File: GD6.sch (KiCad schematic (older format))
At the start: 19 parts, among them IC5 HCPL-316J, IC6 IXDD614PI, P12 CONN_01X03, P13 CONN_01X03

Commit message: uding HCPL-361J modified symbol
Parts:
- IC5: symbol HCPL-316J-RESCUE-gatedrive -> HCPL-316J
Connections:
- wire segments 41 -> 54
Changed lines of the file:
@@
 EESchema Schematic File Version 2
-LIBS:gatedrive-rescue
 LIBS:power
 LIBS:device
@@
 LIBS:contrib
 LIBS:valves
-LIBS:GateDrive
+LIBS:74xgxx
+LIBS:ac-dc
+LIBS:actel
+LIBS:Altera
+LIBS:analog_devices
+LIBS:brooktre
+LIBS:cmos_ieee
+LIBS:dc-dc
+LIBS:diode
+LIBS:elec-unifil
+LIBS:ESD_Protection
+LIBS:ftdi
+LIBS:gennum
+LIBS:graphic
+LIBS:hc11
+LIBS:ir
+LIBS:Lattice
+LIBS:logo
+LIBS:maxim
+LIBS:microchip_dspic33dsc
+LIBS:microchip_pic10mcu
+LIBS:microchip_pic12mcu
+LIBS:microchip_pic16mcu
+LIBS:microchip_pic18mcu
+LIBS:microchip_pic32mcu
+LIBS:motor_drivers
+LIBS:msp430
+LIBS:nordicsemi
+LIBS:nxp_armmcu
+LIBS:onsemi
+LIBS:Oscillators
+LIBS:powerint
+LIBS:Power_Management
+LIBS:pspice
+LIBS:references
+LIBS:relays
+LIBS:rfcom
+LIBS:sensors
+LIBS:silabs
+LIBS:stm8
+LIBS:stm32
+LIBS:supertex
+LIBS:switches
+LIBS:transf
+LIBS:ttl_ieee
+LIBS:video
+LIBS:Worldsemi
+LIBS:Xicor
+LIBS:Zilog
 LIBS:gatedrive-cache
 EELAYER 25 0
@@
 U 1 1 56EF8B77
 P 7900 5100
+AR Path="/56EF8B77" Ref="IC6"  Part="1"
+AR Path="/56EF0565/56EF8B77" Ref="IC6"  Part="1"
 F 0 "IC6" H 7900 4900 60  0000 C CNN
 F 1 "IXDD614PI" H 7950 5450 60  0000 C CNN
@@
 $EndComp
 $Comp
-L HCPL-316J-RESCUE-gatedrive IC5
+L HCPL-316J IC5
 U 1 1 56EF8B78
-P 5550 4750
-F 0 "IC5" H 5550 4150 60  0000 C CNN
-F 1 "HCPL-316J" H 5300 5200 60  0000 C CNN
-F 2 "Housings_SOIC:SOIC-16_7.5x10.3mm_Pitch1.27mm" H 5550 4750 60  0001 C CNN
-F 3 "" H 5550 4750 60  0000 C CNN
-F 4 "CHINA [ already bought]" H 5550 4750 60  0001 C CNN "Supplier"
-	1    5550 4750
+P 5700 4850
+F 0 "IC5" H 5700 4250 60  0000 C CNN
+F 1 "HCPL-316J" H 5450 5300 60  0000 C CNN
+F 2 "Housings_SOIC:SOIC-16_7.5x10.3mm_Pitch1.27mm" H 5700 4850 60  0001 C CNN
+F 3 "" H 5700 4850 60  0000 C CNN
+F 4 "CHINA [ already bought]" H 5700 4850 60  0001 C CNN "Supplier"
+	1    5700 4850
 	1    0    0    -1
 $EndComp
@@
 Text GLabel 7500 5150 0    60   Input ~ 0
 -5V6
-Text GLabel 8350 5150 2    60   Input ~ 0
+Text GLabel 8250 5150 2    60   Input ~ 0
 -5V6
 Text GLabel 10200 4950 2    60   Output ~ 0
@@
 a cap to ensure soft turn-off, recommended by datasheet of hcpl.
 Wire Wire Line
-	6950 4950 7500 4950
-Wire Wire Line
-	6250 4950 6650 4950
-Wire Wire Line
-	6250 5050 6250 5150
-Wire Wire Line
-	6250 4750 6250 4850
+	6950 4950 7150 4950
+Wire Wire Line
+	7150 4950 7500 4950
+Wire Wire Line
+	5900 4950 6500 4950
+Wire Wire Line
+	6500 4950 6650 4950
+Wire Wire Line
+	6250 5050 6250 5100
+Wire Wire Line
+	6250 5100 6250 5150
+Wire Wire Line
+	6250 4750 6250 4800
+Wire Wire Line
+	6250 4800 6250 4850
 Connection ~ 6550 4100
 Wire Wire Line
-	6550 4650 6250 4650
+	6550 4650 5900 4650
 Wire Wire Line
 	6550 4100 6650 4100
 Wire Wire Line
-	6550 4050 6550 4650
+	6550 4050 6550 4100
+Wire Wire Line
+	6550 4100 6550 4650
 Connection ~ 8450 4950
 Wire Wire Line
@@
 Connection ~ 7150 4950
 Wire Wire Line
-	3625 4650 4850 4650
-Wire Wire Line
-	8350 4950 9050 4950
+	3625 4650 4000 4650
+Wire Wire Line
+	4000 4650 5000 4650
+Wire Wire Line
+	8250 4950 8450 4950
+Wire Wire Line
+	8450 4950 8900 4950
+Wire Wire Line
+	8900 4950 9050 4950
 Wire Wire Line
 	9350 4950 9450 4950
 Wire Wire Line
-	9750 4950 10200 4950
+	9750 4950 9950 4950
+Wire Wire Line
+	9950 4950 10200 4950
 Wire Wire Line
 	9750 5250 9950 5250
@@
 Connection ~ 9950 4950
 Wire Wire Line
-	8350 5050 8450 5050
+	8250 5050 8450 5050
 Wire Wire Line
 	8450 5050 8450 4950
@@
 	4400 4350 4400 4550
 Wire Wire Line
-	4400 4550 4850 4550
+	4400 4550 5000 4550
 Wire Wire Line
 	4000 4350 4000 4650
@@
 	4000 5300 4000 4750
 Wire Wire Line
-	4000 4750 4850 4750
-Wire Wire Line
-	4850 5150 4750 5150
+	4000 4750 5000 4750
+Wire Wire Line
+	5000 5150 4750 5150
 Wire Wire Line
 	4750 5150 4750 5300
 Wire Wire Line
-	4850 4850 4400 4850
+	5000 4850 4400 4850
 Wire Wire Line
 	4400 4850 4400 5300
 Wire Wire Line
-	6250 4450 6300 4450
+	5900 4450 6300 4450
 Wire Wire Line
 	6300 4450 6300 4350
@@
 Wire Wire Line
 	6500 5000 6500 4950
-Text GLabel 8350 4850 2    60   Input ~ 0
+Text GLabel 8250 4850 2    60   Input ~ 0
 15V6
 Text GLabel 7025 5125 3    60   Input ~ 0
@@
 Text HLabel 900  3800 3    60   Input ~ 0
 T6
-Text HLabel 4850 4450 0    60   Input ~ 0
+Text HLabel 5000 4450 0    60   Input ~ 0
 T6
 Text GLabel 4450 2300 3    60   Input ~ 0
@@
 Text GLabel 4400 4350 1    60   Input ~ 0
 GND1
-Text GLabel 4850 4950 0    60   Input ~ 0
+Text GLabel 5000 4950 0    60   Input ~ 0
 ~FAULT
 Text GLabel 4750 5300 3    60   Input ~ 0
@@
 Text GLabel 1275 5325 2    60   Input ~ 0
 COM6
+Wire Wire Line
+	6250 4850 5900 4850
+Wire Wire Line
+	6250 4750 5900 4750
+Wire Wire Line
+	6250 5050 5900 5050
+Wire Wire Line
+	6250 5150 5900 5150
 $EndSCHEMATC

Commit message: cleaning the schematic
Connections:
- wire segments 54 -> 45
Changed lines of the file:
@@
 a cap to ensure soft turn-off, recommended by datasheet of hcpl.
 Wire Wire Line
-	6950 4950 7150 4950
+	6950 4950 7500 4950
 Wire Wire Line
-	7150 4950 7500 4950
+	5900 4950 6650 4950
 Wire Wire Line
-	5900 4950 6500 4950
+	6250 5050 6250 5150
 Wire Wire Line
-	6500 4950 6650 4950
-Wire Wire Line
-	6250 5050 6250 5100
-Wire Wire Line
-	6250 5100 6250 5150
-Wire Wire Line
-	6250 4750 6250 4800
-Wire Wire Line
-	6250 4800 6250 4850
+	6250 4750 6250 4850
 Connection ~ 6550 4100
 Wire Wire Line
@@
 	6550 4100 6650 4100
 Wire Wire Line
-	6550 4050 6550 4100
-Wire Wire Line
-	6550 4100 6550 4650
+	6550 4050 6550 4650
 Connection ~ 8450 4950
 Wire Wire Line
@@
 Connection ~ 7150 4950
 Wire Wire Line
-	3625 4650 4000 4650
+	3625 4650 5000 4650
 Wire Wire Line
-	4000 4650 5000 4650
-Wire Wire Line
-	8250 4950 8450 4950
-Wire Wire Line
-	8450 4950 8900 4950
-Wire Wire Line
-	8900 4950 9050 4950
+	8250 4950 9050 4950
 Wire Wire Line
 	9350 4950 9450 4950
 Wire Wire Line
-	9750 4950 9950 4950
-Wire Wire Line
-	9950 4950 10200 4950
+	9750 4950 10200 4950
 Wire Wire Line
 	9750 5250 9950 5250

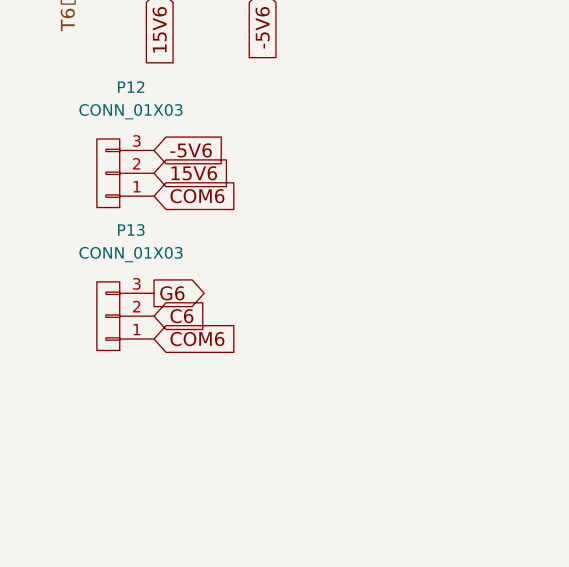
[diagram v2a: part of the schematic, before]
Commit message: completion of the layout, initial layout of the protection circuit, reducing number of circuit to 7
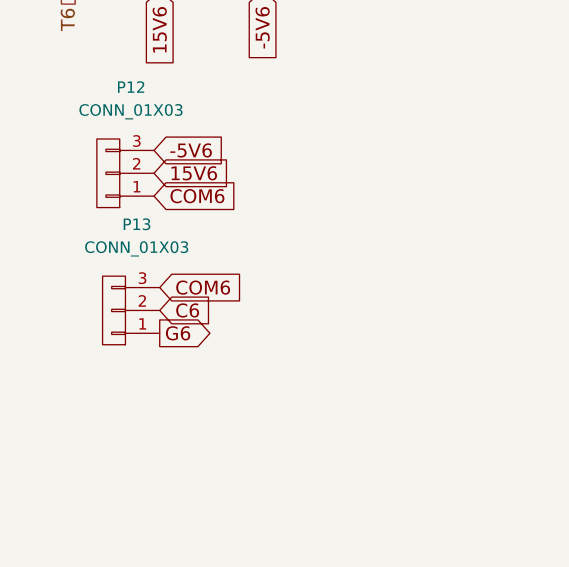
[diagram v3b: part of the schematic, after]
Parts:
- C15, C16, C17, C19, C20, C21: footprint Capacitors_ThroughHole:C_Disc_D3_P2.5 -> gatedrive:C_Disc
- D5: footprint Diodes_ThroughHole:Diode_DO-201AD_Horizontal_RM15 -> Diodes_ThroughHole:Diode_DO-41_SOD81_Horizontal_RM10
- R13: footprint Resistors_ThroughHole:Resistor_Vertical_RM5mm -> Resistors_ThroughHole:Resistor_Horizontal_RM10mm
- R17, R18: footprint Resistors_ThroughHole:Resistor_Horizontal_RM20mm -> gatedrive:Resistor_multi
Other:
- moved on the sheet: P13
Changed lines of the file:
@@
 EESchema Schematic File Version 2
+LIBS:Symbols_DCDC-ACDC-Converter_RevC_20Jul2012
+LIBS:Symbols_EN60617_13Mar2013
+LIBS:Symbols_EN60617-10_HF-Radio_DRAFT_12Sep2013
+LIBS:Symbols_ICs-Diskrete_RevD10
+LIBS:Symbols_ICs-Opto_RevB_16Sep2013
+LIBS:Symbols_Microcontroller_Philips-NXP_RevA_06Oct2013
+LIBS:SymbolsSimilarEN60617+oldDIN617-RevE8
+LIBS:Symbols_Socket-DIN41612_RevA
+LIBS:Symbols_Transformer-Diskrete_RevA
 LIBS:power
 LIBS:device
@@
 $Descr A4 11693 8268
 encoding utf-8
-Sheet 4 10
+Sheet 4 9
 Title "IGBT GATE DRIVE SCHEMATIC."
 Date "2016-03-02"
@@
 F 0 "D5" H 7150 3976 50  0000 C CNN
 F 1 "RGPO2-20" H 7150 3900 50  0000 C CNN
-F 2 "Diodes_ThroughHole:Diode_DO-201AD_Horizontal_RM15" H 7150 4100 50  0001 C CNN
+F 2 "Diodes_ThroughHole:Diode_DO-41_SOD81_Horizontal_RM10" H 7150 4100 50  0001 C CNN
 F 3 "" H 7150 4100 50  0000 C CNN
 F 4 "El-Amir" H 7150 4100 60  0001 C CNN "Supplier"
@@
 F 0 "R13" V 3525 4500 50  0000 C CNN
 F 1 "10K" V 3625 4500 50  0000 C CNN
-F 2 "Resistors_ThroughHole:Resistor_Vertical_RM5mm" V 3555 4500 50  0001 C CNN
+F 2 "Resistors_ThroughHole:Resistor_Horizontal_RM10mm" V 3555 4500 50  0001 C CNN
 F 3 "" H 3625 4500 50  0000 C CNN
 F 4 "EL AMIR" H 3625 4500 60  0001 C CNN "Supplier"
@@
 F 0 "C15" H 4150 2150 50  0000 C CNN
 F 1 "0.1uF" H 4250 2050 50  0000 C CNN
-F 2 "Capacitors_ThroughHole:C_Disc_D3_P2.5" H 4488 2000 50  0001 C CNN
+F 2 "gatedrive:C_Disc" H 4488 2000 50  0001 C CNN
 F 3 "" H 4450 2150 50  0000 C CNN
 F 4 "EL AMIR" H 4450 2150 60  0001 C CNN "Supplier"
@@
 F 0 "C17" H 7000 3900 50  0000 C CNN
 F 1 "100pF" H 6800 3900 50  0000 C CNN
-F 2 "Capacitors_ThroughHole:C_Disc_D3_P2.5" H 6588 3750 50  0001 C CNN
+F 2 "gatedrive:C_Disc" H 6588 3750 50  0001 C CNN
 F 3 "" H 6550 3900 50  0000 C CNN
 	1    6550 3900
@@
 F 0 "C21" H 8450 2150 50  0000 C CNN
 F 1 "0.1uF" H 8450 2050 50  0000 C CNN
-F 2 "Capacitors_ThroughHole:C_Disc_D3_P2.5" H 8888 2000 50  0001 C CNN
+F 2 "gatedrive:C_Disc" H 8888 2000 50  0001 C CNN
 F 3 "" H 8850 2150 50  0000 C CNN
 	1    8850 2150
@@
 F 0 "C20" H 7400 2150 50  0000 C CNN
 F 1 "0.1uF" H 7400 2050 50  0000 C CNN
-F 2 "Capacitors_ThroughHole:C_Disc_D3_P2.5" H 7788 2000 50  0001 C CNN
+F 2 "gatedrive:C_Disc" H 7788 2000 50  0001 C CNN
 F 3 "" H 7750 2150 50  0000 C CNN
 	1    7750 2150
@@
 F 0 "C16" H 5150 2150 50  0000 C CNN
 F 1 "0.1uF" H 5150 2050 50  0000 C CNN
-F 2 "Capacitors_ThroughHole:C_Disc_D3_P2.5" H 5538 2000 50  0001 C CNN
+F 2 "gatedrive:C_Disc" H 5538 2000 50  0001 C CNN
 F 3 "" H 5500 2150 50  0000 C CNN
 	1    5500 2150
@@
 LEFT OPEN OR CONNECTED TO THE VCC.
 $Comp
-L PWR_FLAG #FLG015
+L PWR_FLAG #FLG08
 U 1 1 56EF8B85
 P 1300 3800
-F 0 "#FLG015" H 1300 3895 50  0001 C CNN
+F 0 "#FLG08" H 1300 3895 50  0001 C CNN
 F 1 "PWR_FLAG" H 1300 4024 50  0000 C CNN
 F 2 "" H 1300 3800 50  0000 C CNN
@@
 $EndComp
 $Comp
-L PWR_FLAG #FLG016
+L PWR_FLAG #FLG09
 U 1 1 56EF8B86
 P 1750 3800
-F 0 "#FLG016" H 1750 3895 50  0001 C CNN
+F 0 "#FLG09" H 1750 3895 50  0001 C CNN
 F 1 "PWR_FLAG" H 1750 4024 50  0000 C CNN
 F 2 "" H 1750 3800 50  0000 C CNN
@@
 $EndComp
 $Comp
-L PWR_FLAG #FLG017
+L PWR_FLAG #FLG010
 U 1 1 56EF8B87
 P 1750 2650
-F 0 "#FLG017" H 1750 2745 50  0001 C CNN
+F 0 "#FLG010" H 1750 2745 50  0001 C CNN
 F 1 "PWR_FLAG" H 1750 2874 50  0000 C CNN
 F 2 "" H 1750 2650 50  0000 C CNN
@@
 $EndComp
 $Comp
-L PWR_FLAG #FLG018
+L PWR_FLAG #FLG011
 U 1 1 56EF8B88
 P 900 2650
-F 0 "#FLG018" H 900 2745 50  0001 C CNN
+F 0 "#FLG011" H 900 2745 50  0001 C CNN
 F 1 "PWR_FLAG" H 900 2874 50  0000 C CNN
 F 2 "" H 900 2650 50  0000 C CNN
@@
 $EndComp
 $Comp
-L PWR_FLAG #FLG019
+L PWR_FLAG #FLG012
 U 1 1 56EF8B89
 P 1300 2650
-F 0 "#FLG019" H 1300 2745 50  0001 C CNN
+F 0 "#FLG012" H 1300 2745 50  0001 C CNN
 F 1 "PWR_FLAG" H 1300 2874 50  0000 C CNN
 F 2 "" H 1300 2650 50  0000 C CNN
@@
 $EndComp
 $Comp
-L PWR_FLAG #FLG020
+L PWR_FLAG #FLG013
 U 1 1 56EF8B8A
 P 900 3800
-F 0 "#FLG020" H 900 3895 50  0001 C CNN
+F 0 "#FLG013" H 900 3895 50  0001 C CNN
 F 1 "PWR_FLAG" H 900 4024 50  0000 C CNN
 F 2 "" H 900 3800 50  0000 C CNN
@@
 F 0 "C19" H 7390 4630 50  0000 C CNN
 F 1 "10nF" H 7400 4550 50  0000 C CNN
-F 2 "Capacitors_ThroughHole:C_Disc_D3_P2.5" H 7188 4450 50  0001 C CNN
+F 2 "gatedrive:C_Disc" H 7188 4450 50  0001 C CNN
 F 3 "" H 7150 4600 50  0000 C CNN
 	1    7150 4600
@@
 F 0 "R17" V 9600 4980 50  0000 C CNN
 F 1 "60" V 9500 4950 50  0000 C CNN
-F 2 "Resistors_ThroughHole:Resistor_Horizontal_RM20mm" V 9530 4950 50  0001 C CNN
+F 2 "gatedrive:Resistor_multi" V 9530 4950 50  0001 C CNN
 F 3 "" H 9600 4950 50  0000 C CNN
 F 4 "Al amir" H 9600 4950 60  0001 C CNN "Supplier"
@@
 F 0 "R18" V 9600 5240 50  0000 C CNN
 F 1 "30ohm ,0.5W" V 9500 5250 50  0000 C CNN
-F 2 "Resistors_ThroughHole:Resistor_Horizontal_RM20mm" V 9530 5250 50  0001 C CNN
+F 2 "gatedrive:Resistor_multi" V 9530 5250 50  0001 C CNN
 F 3 "" H 9600 5250 50  0000 C CNN
 F 4 "Supplier_name" H 9600 5250 60  0001 C CNN "Supplier"
@@
 	6950 4100 7000 4100
 $Comp
-L PWR_FLAG #FLG021
+L PWR_FLAG #FLG014
 U 1 1 56EF8B91
 P 1475 3050
-F 0 "#FLG021" H 1475 3145 50  0001 C CNN
+F 0 "#FLG014" H 1475 3145 50  0001 C CNN
 F 1 "PWR_FLAG" V 1625 3050 50  0000 C CNN
 F 2 "" H 1475 3050 50  0000 C CNN
@@
 L CONN_01X03 P13
 U 1 1 56F6B56E
-P 1075 5225
-F 0 "P13" H 975 4850 50  0000 C CNN
-F 1 "CONN_01X03" H 975 4950 50  0000 C CNN
-F 2 "Pin_Headers:Pin_Header_Angled_1x03" H 1075 5225 50  0001 C CNN
-F 3 "" H 1075 5225 50  0000 C CNN
-	1    1075 5225
+P 1100 5200
+F 0 "P13" H 1000 4825 50  0000 C CNN
+F 1 "CONN_01X03" H 1000 4925 50  0000 C CNN
+F 2 "Pin_Headers:Pin_Header_Angled_1x03" H 1100 5200 50  0001 C CNN
+F 3 "" H 1100 5200 50  0000 C CNN
+	1    1100 5200
 	-1   0    0    1
 $EndComp
@@
 Text GLabel 1275 4500 2    60   Input ~ 0
 -5V6
-Text GLabel 1275 5125 2    60   Output ~ 0
+Text GLabel 1300 5300 2    60   Output ~ 0
 G6
-Text GLabel 1275 5225 2    60   Input ~ 0
+Text GLabel 1300 5200 2    60   Input ~ 0
 C6
-Text GLabel 1275 5325 2    60   Input ~ 0
+Text GLabel 1300 5100 2    60   Input ~ 0
 COM6
 Wire Wire Line

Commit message: yet another enhancements .
the protection section still is incomplete.
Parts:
- IC6: symbol IXDD614PI-RESCUE-gatedrive -> IXDD614PI
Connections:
- wire segments 45 -> 54
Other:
- moved on the sheet: IC5
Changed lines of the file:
@@
 $Descr A4 11693 8268
 encoding utf-8
-Sheet 4 9
+Sheet 3 9
 Title "IGBT GATE DRIVE SCHEMATIC."
 Date "2016-03-02"
@@
 $EndDescr
 $Comp
-L IXDD614PI-RESCUE-gatedrive IC6
+L IXDD614PI IC6
 U 1 1 56EF8B77
-P 7900 5100
+P 7900 4950
 AR Path="/56EF8B77" Ref="IC6"  Part="1"
 AR Path="/56EF0565/56EF8B77" Ref="IC6"  Part="1"
-F 0 "IC6" H 7900 4900 60  0000 C CNN
-F 1 "IXDD614PI" H 7950 5450 60  0000 C CNN
-F 2 "gatedrive:DIP-8_W7.62mm_LongPads" H 7900 5200 60  0001 C CNN
-F 3 "" H 7900 5200 60  0000 C CNN
-F 4 "CHINA[already bought]" H 7900 5100 60  0001 C CNN "Supplier"
-	1    7900 5100
+F 0 "IC6" H 7900 4750 60  0000 C CNN
+F 1 "IXDD614PI" H 7950 5300 60  0000 C CNN
+F 2 "gatedrive:DIP-8_W7.62mm_LongPads" H 7900 5050 60  0001 C CNN
+F 3 "" H 7900 5050 60  0000 C CNN
+F 4 "CHINA[already bought]" H 7900 4950 60  0001 C CNN "Supplier"
+	1    7900 4950
 	1    0    0    -1
 $EndComp
@@
 L HCPL-316J IC5
 U 1 1 56EF8B78
-P 5700 4850
-F 0 "IC5" H 5700 4250 60  0000 C CNN
-F 1 "HCPL-316J" H 5450 5300 60  0000 C CNN
-F 2 "Housings_SOIC:SOIC-16_7.5x10.3mm_Pitch1.27mm" H 5700 4850 60  0001 C CNN
-F 3 "" H 5700 4850 60  0000 C CNN
-F 4 "CHINA [ already bought]" H 5700 4850 60  0001 C CNN "Supplier"
-	1    5700 4850
+P 5400 4750
+AR Path="/56EF8B78" Ref="IC5"  Part="1"
+AR Path="/56EF0565/56EF8B78" Ref="IC5"  Part="1"
+F 0 "IC5" H 5400 4150 60  0000 C CNN
+F 1 "HCPL-316J" H 5150 5200 60  0000 C CNN
+F 2 "Housings_SOIC:SOIC-16_7.5x10.3mm_Pitch1.27mm" H 5400 4750 60  0001 C CNN
+F 3 "" H 5400 4750 60  0000 C CNN
+F 4 "CHINA [ already bought]" H 5400 4750 60  0001 C CNN "Supplier"
+	1    5400 4750
 	1    0    0    -1
 $EndComp
@@
 Text GLabel 7500 5150 0    60   Input ~ 0
 -5V6
-Text GLabel 8250 5150 2    60   Input ~ 0
+Text GLabel 8300 5150 2    60   Input ~ 0
 -5V6
 Text GLabel 10200 4950 2    60   Output ~ 0
@@
 a cap to ensure soft turn-off, recommended by datasheet of hcpl.
 Wire Wire Line
-	6950 4950 7500 4950
-Wire Wire Line
-	5900 4950 6650 4950
-Wire Wire Line
-	6250 5050 6250 5150
-Wire Wire Line
-	6250 4750 6250 4850
+	6950 4950 7150 4950
+Wire Wire Line
+	7150 4950 7500 4950
+Wire Wire Line
+	5900 4950 6500 4950
+Wire Wire Line
+	6500 4950 6650 4950
+Wire Wire Line
+	6250 5050 6250 5100
+Wire Wire Line
+	6250 5100 6250 5150
+Wire Wire Line
+	6250 4750 6250 4800
+Wire Wire Line
+	6250 4800 6250 4850
 Connection ~ 6550 4100
 Wire Wire Line
@@
 	6550 4100 6650 4100
 Wire Wire Line
-	6550 4050 6550 4650
+	6550 4050 6550 4100
+Wire Wire Line
+	6550 4100 6550 4650
 Connection ~ 8450 4950
 Wire Wire Line
@@
 Connection ~ 7150 4950
 Wire Wire Line
-	3625 4650 5000 4650
-Wire Wire Line
-	8250 4950 9050 4950
+	3625 4650 4000 4650
+Wire Wire Line
+	4000 4650 4900 4650
+Wire Wire Line
+	8300 4950 8450 4950
+Wire Wire Line
+	8450 4950 8900 4950
+Wire Wire Line
+	8900 4950 9050 4950
 Wire Wire Line
 	9350 4950 9450 4950
 Wire Wire Line
-	9750 4950 10200 4950
+	9750 4950 9950 4950
+Wire Wire Line
+	9950 4950 10200 4950
 Wire Wire Line
 	9750 5250 9950 5250
@@
 Connection ~ 9950 4950
 Wire Wire Line
-	8250 5050 8450 5050
+	8300 5050 8450 5050
 Wire Wire Line
 	8450 5050 8450 4950
@@
 	4400 4350 4400 4550
 Wire Wire Line
-	4400 4550 5000 4550
+	4400 4550 4900 4550
 Wire Wire Line
 	4000 4350 4000 4650
@@
 	4000 5300 4000 4750
 Wire Wire Line
-	4000 4750 5000 4750
-Wire Wire Line
-	5000 5150 4750 5150
+	4000 4750 4900 4750
+Wire Wire Line
+	4900 5150 4750 5150
 Wire Wire Line
 	4750 5150 4750 5300
 Wire Wire Line
-	5000 4850 4400 4850
+	4900 4850 4400 4850
 Wire Wire Line
 	4400 4850 4400 5300
@@
 Wire Wire Line
 	6500 5000 6500 4950
-Text GLabel 8250 4850 2    60   Input ~ 0
+Text GLabel 8300 4850 2    60   Input ~ 0
 15V6
 Text GLabel 7025 5125 3    60   Input ~ 0
@@
 Text HLabel 900  3800 3    60   Input ~ 0
 T6
-Text HLabel 5000 4450 0    60   Input ~ 0
+Text HLabel 4900 4450 0    60   Input ~ 0
 T6
 Text GLabel 4450 2300 3    60   Input ~ 0
@@
 Text GLabel 4400 4350 1    60   Input ~ 0
 GND1
-Text GLabel 5000 4950 0    60   Input ~ 0
+Text GLabel 4900 4950 0    60   Input ~ 0
 ~FAULT
 Text GLabel 4750 5300 3    60   Input ~ 0

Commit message: packup
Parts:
- removed C15, C16, C20, C21: 0.1uF, gatedrive:C_Disc, symbol CP1
- removed C17: 100pF, gatedrive:C_Disc, symbol CP1
- removed C18: 330pF, Capacitors_ThroughHole:C_Disc_D3_P2.5, symbol CP1
- removed C19: 10nF, gatedrive:C_Disc, symbol CP1
- removed D5: RGPO2-20, Diodes_ThroughHole:Diode_DO-41_SOD81_Horizontal_RM10, symbol D
- removed D6: ~, Diodes_ThroughHole:Diode_DO-201AD_Horizontal_RM15, symbol D
- removed IC5: HCPL-316J, Housings_SOIC:SOIC-16_7.5x10.3mm_Pitch1.27mm, symbol HCPL-316J
- removed IC6: IXDD614PI, gatedrive:DIP-8_W7.62mm_LongPads, symbol IXDD614PI
- removed P12, P13: CONN_01X03, Pin_Headers:Pin_Header_Angled_1x03, symbol CONN_01X03
- removed R13: 10K, Resistors_ThroughHole:Resistor_Horizontal_RM10mm, symbol R
- removed R14: 25K, Resistors_ThroughHole:Resistor_Horizontal_RM10mm, symbol R
- removed R15, R16: 100, Resistors_ThroughHole:Resistor_Horizontal_RM10mm, symbol R
- removed R17: 60, gatedrive:Resistor_multi, symbol R
- removed R18: 30ohm ,0.5W, gatedrive:Resistor_multi, symbol R
- added C301, C303, C304, C305: 0.1uF, gatedrive:C_Disc, symbol C_Small
- added C302: 330pF, gatedrive:C_Disc, symbol C_Small
- added C306: 100pF, gatedrive:C_Disc, symbol C_Small
- added C307: 10nF, gatedrive:C_Disc, symbol C_Small
- added D301: RGPO2-20, Diodes_ThroughHole:Diode_DO-41_SOD81_Horizontal_RM10, symbol D
- added D302: ~, Diodes_ThroughHole:Diode_DO-201AD_Horizontal_RM15, symbol D
- added IC301: HCPL-316J, Housings_SOIC:SOIC-16_7.5x10.3mm_Pitch1.27mm, symbol HCPL-316J
- added IC302: IXDD614PI, gatedrive:DIP-8_W7.62mm_LongPads, symbol IXDD614PI
- added P301, P302: CONN_01X03, gatedrive:conn, symbol CONN_01X03
- added R301: 10K, Resistors_ThroughHole:Resistor_Horizontal_RM10mm, symbol R_Small
- added R302: 25K, Resistors_ThroughHole:Resistor_Horizontal_RM10mm, symbol R_Small
- added R303, R304: 100, Resistors_ThroughHole:Resistor_Horizontal_RM10mm, symbol R_Small
- added R305: 60, gatedrive:Resistor_multi, symbol R_Small
- added R306: 30ohm ,0.5W, gatedrive:Resistor_multi, symbol R_Small
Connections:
- net 15V6: now also C304.2, C305.1, IC301.12 (Vc), IC301.13 (Vcc2), IC302.1 (VCC), IC302.3 (EN), IC302.8 (VCC), P301.2 (P2)
- net COM6: now also C303.2, C304.1, C306.2, IC301.16 (VE), P301.1 (P1), P302.3 (P3)
- net G6: now also P302.1 (P1), R305.2, R306.2
- net T6: now also IC301.1 (Vin+)
- net ~FAULT: now also C302.1, IC301.6 (~FAULT), R301.1
- net ~RST: now also IC301.5 (~RESET)
- new net: IC301.11 (Vout), R302.2, R304.2
- new net: C306.1, IC301.14 (DESAT), R303.1
- new net: C307.1, IC302.2 (IN), R304.1
- new net: D301.2 (A), R303.2
- new net: D302.1 (K), R305.1
- new net: D302.2 (A), IC302.6 (OUT), IC302.7 (OUT), R306.1
- new net +5V: C301.1, IC301.3 (Vcc1), R301.2
- new net -5v6: C303.1, C305.2, C307.2, IC301.10 (VEE), IC301.9 (VEE), IC302.4 (GND), IC302.5 (GND), P301.3 (P3), R302.1
- new net GND: C301.2, C302.2, IC301.2 (Vin-), IC301.4 (GND1), IC301.8 (Vled1-)
- new net c6: D301.1 (K), P302.2 (P2)
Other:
- note added: "5 volt is the vcc of the microcontroller.\n"
- note added: "GND is the ground of the microcontroller.\n"
- note added: "IN PIN IS LEFT OPEN OR CONNECTED TO THE VCC."
- note added: "a cap to ensure soft turn-off,\n recommended by datasheet of hcpl."
- note removed: "Fault pull-up resistor."
- note removed: "GND1 is the ground of the microcontroller.\n"
- note removed: "I'M USING GLOBAL LABELS INSTEAD OF LOCAL LABELS AS THEY LOOK NEATER, LOL."
- note removed: "LEFT OPEN OR CONNECTED TO THE VCC."
- note removed: "MICSUPP is 5 volt from the vcc of the microcontroller.\n"
- note removed: "a cap to ensure soft turn-off, recommended by datasheet of hcpl."
